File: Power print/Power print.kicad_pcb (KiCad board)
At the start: 2 copper layers, 38 parts, among them IC1 INA3221AIRGVR, IC2 TPS566247DRLR, J2 Microcontroller, J3 Vout_Connector, J4 USB_C_Receptacle_USB2.0_16P, Q1 BSS123, Q2 ZXMP4A16G, SW1 SW_Push, U1 CH224K

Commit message: PCB design
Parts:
- removed R16: 10K, Resistor_SMD:R_1206_3216Metric_Pad1.30x1.75mm_HandSolder
- removed SW1: SW_Push, Connector_PinHeader_2.54mm:PinHeader_1x02_P2.54mm_Vertical
- added J1: Conn_01x03_Pin, Connector_PinHeader_1.00mm:PinHeader_1x03_P1.00mm_Vertical, F.Cu at (75.2, 117.3)
- added REF**: OSHW-Logo_7.5x8mm_SilkScreen, Symbol:OSHW-Logo_7.5x8mm_SilkScreen, F.Cu at (130.8, 110.2)
- added REF**: MountingHole_3.2mm_M3, MountingHole:MountingHole_3.2mm_M3, F.Cu at (50.0, 90.4)
- added REF**: MountingHole_3.2mm_M3, MountingHole:MountingHole_3.2mm_M3, F.Cu at (140.7, 90.4)
- added REF**: MountingHole_3.2mm_M3, MountingHole:MountingHole_3.2mm_M3, F.Cu at (140.7, 115.6)
- added REF**: MountingHole_3.2mm_M3, MountingHole:MountingHole_3.2mm_M3, F.Cu at (50.0, 115.6)
- IC2: footprint PCBLIB_SOT-5X3-6_W1.6-L1.2-P0.50-LS1.6-BL_2024-11-15:SOT-5X3-6_W1.6-L1.2-P0.50-LS1.6-BL -> Package_TO_SOT_SMD:SOT-563
- J2: value Microcontroller -> Conn_01x07_Pin; footprint Connector_PinHeader_2.54mm:PinHeader_2x05_P2.54mm_Vertical -> Connector_PinHeader_1.00mm:PinHeader_1x07_P1.00mm_Vertical
- moved R15 50.8 mm to (111.8, 107.1), turned to -90 degrees
- moved R17 45.9 mm to (116.8, 107.2), turned to -90 degrees
- moved R21 45.0 mm to (112.8, 113.6), turned to 90 degrees
- moved IC1 40.0 mm to (101.9, 107.1)
- moved C9 39.8 mm to (96.5, 107.5), turned to 90 degrees
- moved R18 37.0 mm to (108.5, 113.6), turned to 90 degrees
- moved C3 35.3 mm to (99.6, 90.4), turned to -90 degrees
- moved C2 35.2 mm to (94.2, 90.4), turned to -90 degrees
- moved D1 29.0 mm to (74.2, 100.7)
- moved R19 27.7 mm to (96.5, 113.6), turned to 90 degrees
- moved Q1 26.3 mm to (80.8, 100.6)
- moved R5 26.2 mm to (131.6, 100.8), turned to 90 degrees
- moved R20 25.9 mm to (91.4, 113.6), turned to 90 degrees
- moved J3 23.9 mm to (140.0, 102.4), turned to -90 degrees
- moved IC2 22.3 mm to (110.5, 93.0)
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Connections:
- D1 pad 3: Net-(D1-Pad3) -> SW1
- IC1 pad 13: TC -> unconnected-(IC1-TC-Pad13)
- J2 pad 2: PV -> SCL
- J2 pad 3: uController -> SDA
- J2 pad 4: TC -> Warning
- J2 pad 5: SCL -> Critical
- J2 pad 6: Warning -> PV
- J2 pad 7: SDA -> GND
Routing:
- net Vin_n_2: track 0.00 -> 108.9 mm, vias 0 -> 2
- net Vbus: track 0.00 -> 84.7 mm, vias 0 -> 2
- net Vin_p_1: track 0.00 -> 77.9 mm, vias 0 -> 6
- net Vin_p_2: track 0.00 -> 58.3 mm, vias 0 -> 2
- net GND: track 0.00 -> 46.8 mm, vias 0 -> 105
- net Net-(U1-DM): track 0.00 -> 33.2 mm
- net Vbuck: track 0.00 -> 32.9 mm
- net Net-(Q1-D): track 0.00 -> 31.8 mm, vias 0 -> 2
- net PV: track 0.00 -> 31.0 mm
- net Net-(U1-DP): track 0.00 -> 30.9 mm
- net Net-(J4-CC2): track 0.00 -> 28.8 mm
- net Net-(U1-VDD): track 0.00 -> 24.2 mm
- net Critical: track 0.00 -> 24.0 mm
- net SCL: track 0.00 -> 23.7 mm
- net Net-(IC1-VPU): track 0.00 -> 22.2 mm, vias 0 -> 2
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- added copper zone on B.Cu, net GND
- added copper zone on F.Cu, net GND
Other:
- board outline added: 100.1 x 34.8 mm
- board text added: "5V"
- board text added: "Crit"
- board text added: "Cryptable Cyberdeck PMGNT v1.0"
- board text added: "GND"
- board text added: "MCU"
- board text added: "PV"
- board text added: "SCL"
- board text added: "SDA"
- board text added: "SW1"
- board text added: "SW2"
- board text added: "Warn"

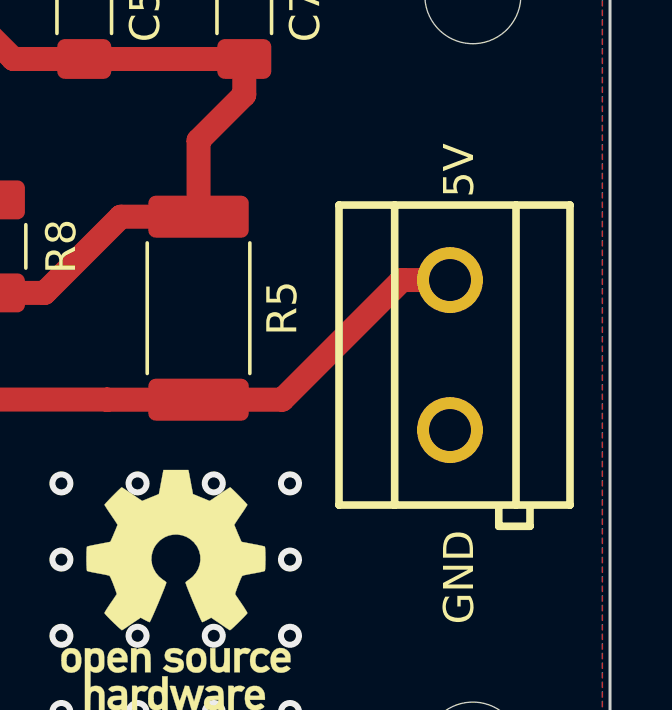
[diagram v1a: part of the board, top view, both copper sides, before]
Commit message: Rotated power connector
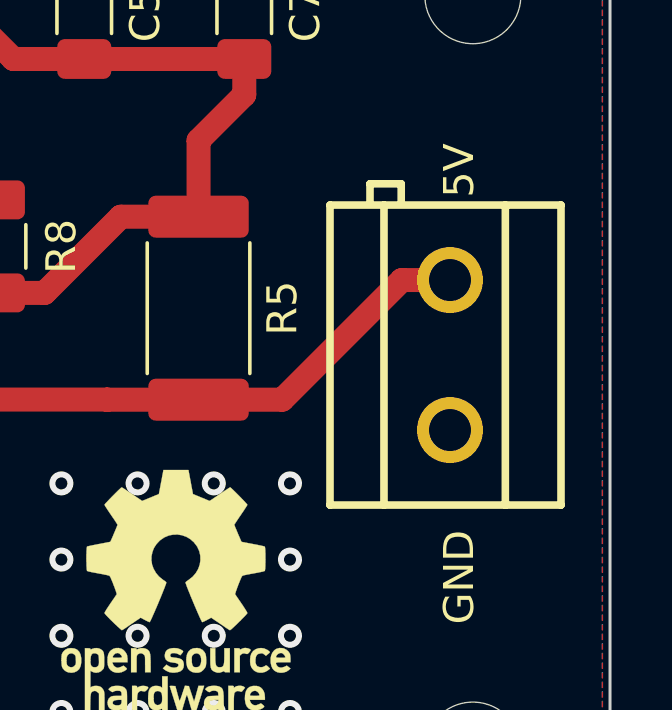
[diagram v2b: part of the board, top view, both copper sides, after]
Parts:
- turned J3 to 90 degrees
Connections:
- J3 pad 1: Vin_n_2 -> GND
- J3 pad 2: GND -> Vin_n_2
